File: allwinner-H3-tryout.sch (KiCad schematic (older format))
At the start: 0 parts

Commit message: update,
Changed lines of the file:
@@
 $Descr A4 11693 8268
 encoding utf-8
-Sheet 1 10
+Sheet 1 12
 Title ""
 Date ""
@@
 $EndSheet
 $Sheet
-S 7750 1100 1050 900
+S 8150 1100 1050 900
 U 5C7849B0
 F0 "POWER" 50
@@
 $EndSheet
 $Sheet
-S 7350 4750 1050 900
+S 8150 4750 1050 900
 U 5C1FD862
 F0 "IR" 50
@@
 $EndSheet
 $Sheet
-S 5750 4750 1050 900
+S 6900 4750 1050 900
 U 5C2139DD
 F0 "UART0" 50
@@
 $EndSheet
 $Sheet
-S 4400 4750 1050 900
+S 5650 4750 1050 900
 U 5C21AE0A
 F0 "RTC" 50
@@
 F1 "CSI.sch" 50
 $EndSheet
+$Sheet
+S 8150 2300 1050 900
+U 5C21B42E
+F0 "TF" 50
+F1 "TF.sch" 50
+$EndSheet
+$Sheet
+S 6900 1100 1050 900
+U 5C22EE91
+F0 "USB_POWER" 50
+F1 "USB_POWER.sch" 50
+$EndSheet
+$Sheet
+S 5250 1100 1050 900
+U 5C22DA43
+F0 "eMMC" 50
+F1 "eMMC.sch" 50
+$EndSheet
 $EndSCHEMATC

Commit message: update,
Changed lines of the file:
@@
 $Descr A4 11693 8268
 encoding utf-8
-Sheet 1 12
+Sheet 1 14
 Title ""
 Date ""
@@
 $EndSheet
 $Sheet
-S 5250 1100 1050 900
+S 5650 1100 1050 900
 U 5C22DA43
 F0 "eMMC" 50
 F1 "eMMC.sch" 50
 $EndSheet
+$Sheet
+S 4400 1100 1050 900
+U 5C23FAEA
+F0 "dram" 50
+F1 "dram.sch" 50
+$EndSheet
 $EndSCHEMATC

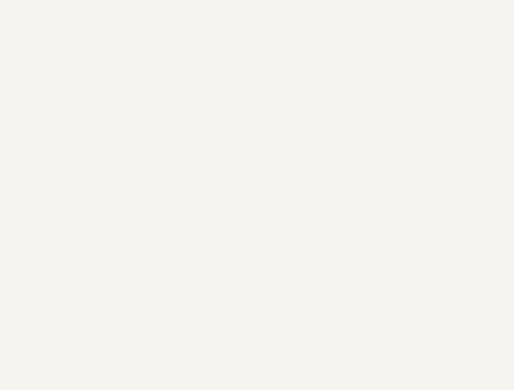
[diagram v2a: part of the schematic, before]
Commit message: udpate mounting hole,
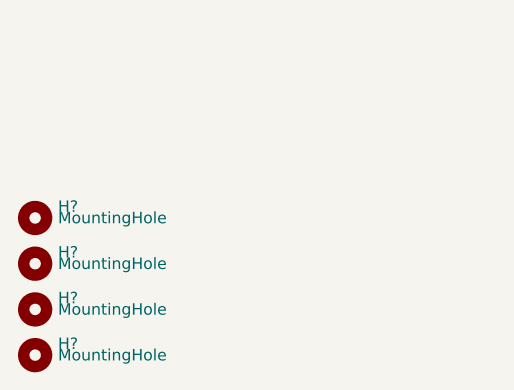
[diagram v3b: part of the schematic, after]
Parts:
- added H? (x3): MountingHole, MountingHole:MountingHole_2.2mm_M2_DIN965, symbol Mechanical:MountingHole
- added H?: MountingHole, MountingHole:MountingHole_2MountingHole:MountingHole_2.2mm_M2_DIN965.2mm_M2_DIN965, symbol Mechanical:MountingHole
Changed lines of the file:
@@
 F1 "dram.sch" 50
 $EndSheet
+$Comp
+L Mechanical:MountingHole H?
+U 1 1 5C5BD210
+P 3950 7000
+F 0 "H?" H 4050 7050 50  0000 L CNN
+F 1 "MountingHole" H 4050 7000 50  0000 L CNN
+F 2 "MountingHole:MountingHole_2.2mm_M2_DIN965" H 3950 7000 50  0001 C CNN
+F 3 "~" H 3950 7000 50  0001 C CNN
+	1    3950 7000
+	1    0    0    -1
+$EndComp
+$Comp
+L Mechanical:MountingHole H?
+U 1 1 5C5BD268
+P 3950 7200
+F 0 "H?" H 4050 7250 50  0000 L CNN
+F 1 "MountingHole" H 4050 7200 50  0000 L CNN
+F 2 "MountingHole:MountingHole_2.2mm_M2_DIN965" H 3950 7200 50  0001 C CNN
+F 3 "~" H 3950 7200 50  0001 C CNN
+	1    3950 7200
+	1    0    0    -1
+$EndComp
+$Comp
+L Mechanical:MountingHole H?
+U 1 1 5C5BD298
+P 3950 7400
+F 0 "H?" H 4050 7450 50  0000 L CNN
+F 1 "MountingHole" H 4050 7400 50  0000 L CNN
+F 2 "MountingHole:MountingHole_2.2mm_M2_DIN965" H 3950 7400 50  0001 C CNN
+F 3 "~" H 3950 7400 50  0001 C CNN
+	1    3950 7400
+	1    0    0    -1
+$EndComp
+$Comp
+L Mechanical:MountingHole H?
+U 1 1 5C5BD2C2
+P 3950 7600
+F 0 "H?" H 4050 7650 50  0000 L CNN
+F 1 "MountingHole" H 4050 7600 50  0000 L CNN
+F 2 "MountingHole:MountingHole_2MountingHole:MountingHole_2.2mm_M2_DIN965.2mm_M2_DIN965" H 3950 7600 50  0001 C CNN
+F 3 "~" H 3950 7600 50  0001 C CNN
+	1    3950 7600
+	1    0    0    -1
+$EndComp
 $EndSCHEMATC

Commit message: update,
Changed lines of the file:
@@
 $Descr A4 11693 8268
 encoding utf-8
-Sheet 1 14
+Sheet 1 15
 Title ""
 Date ""
@@
 	1    0    0    -1
 $EndComp
+$Sheet
+S 600  650  850  400
+U 5C5C55F2
+F0 "cpu-power" 50
+F1 "cpu-power.sch" 50
+$EndSheet
 $EndSCHEMATC

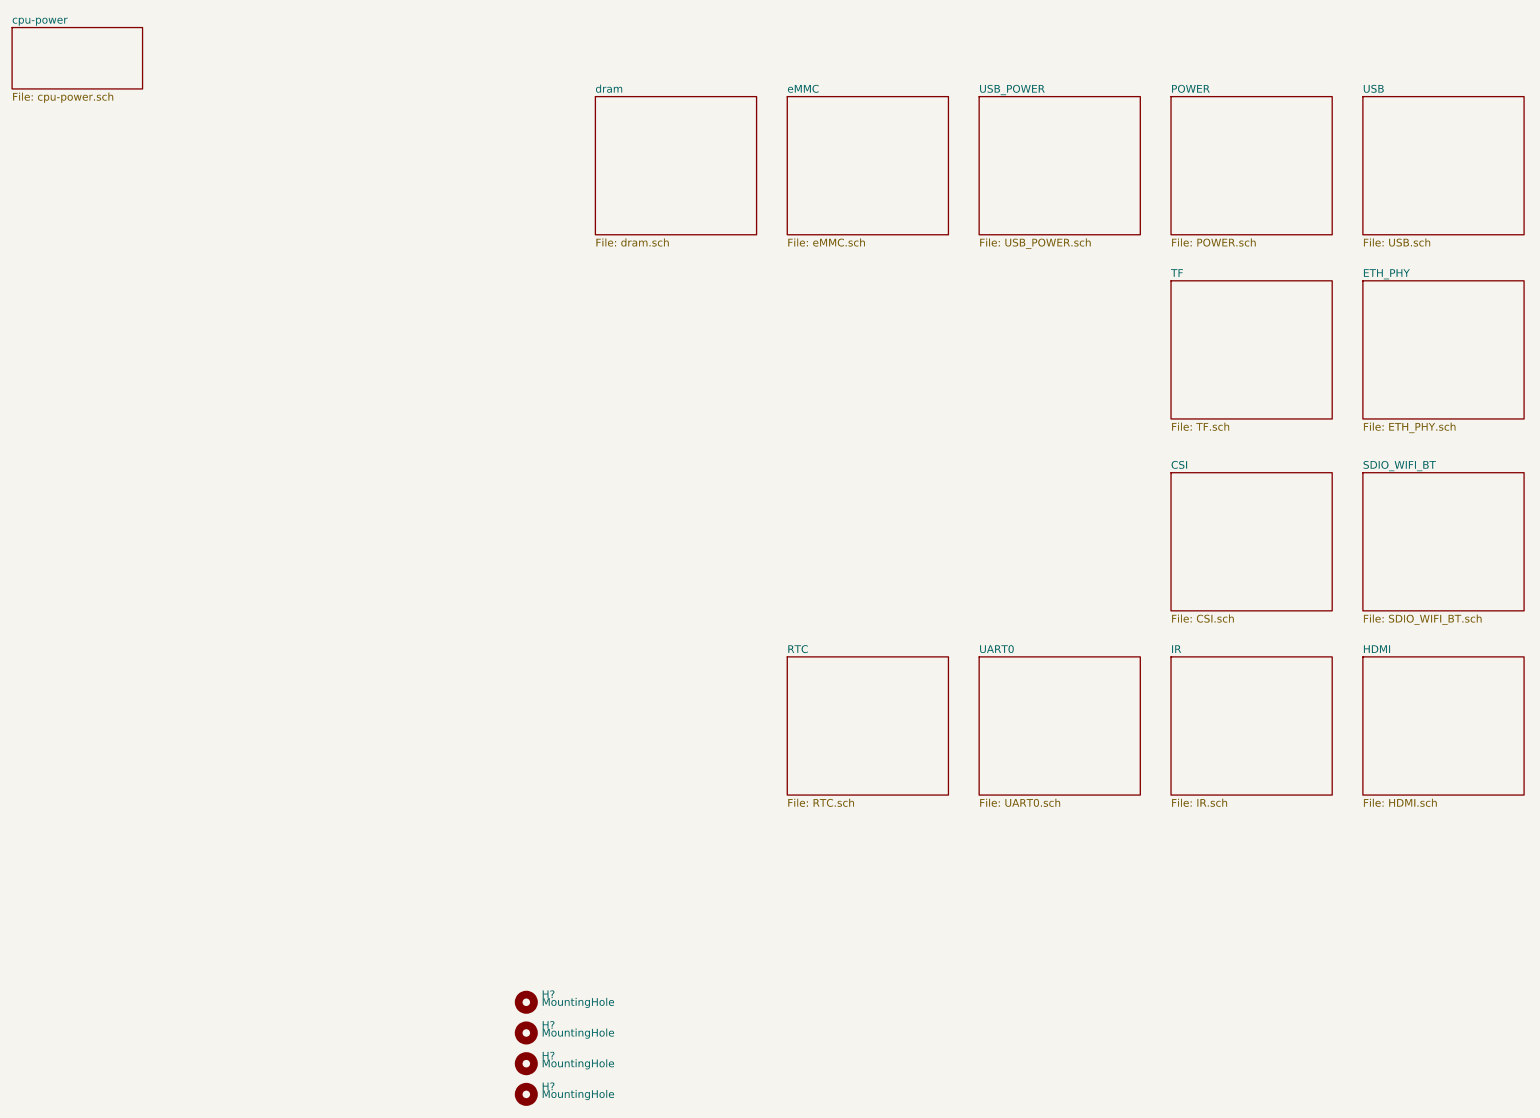
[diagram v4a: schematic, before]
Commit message: update cpu related schematic,
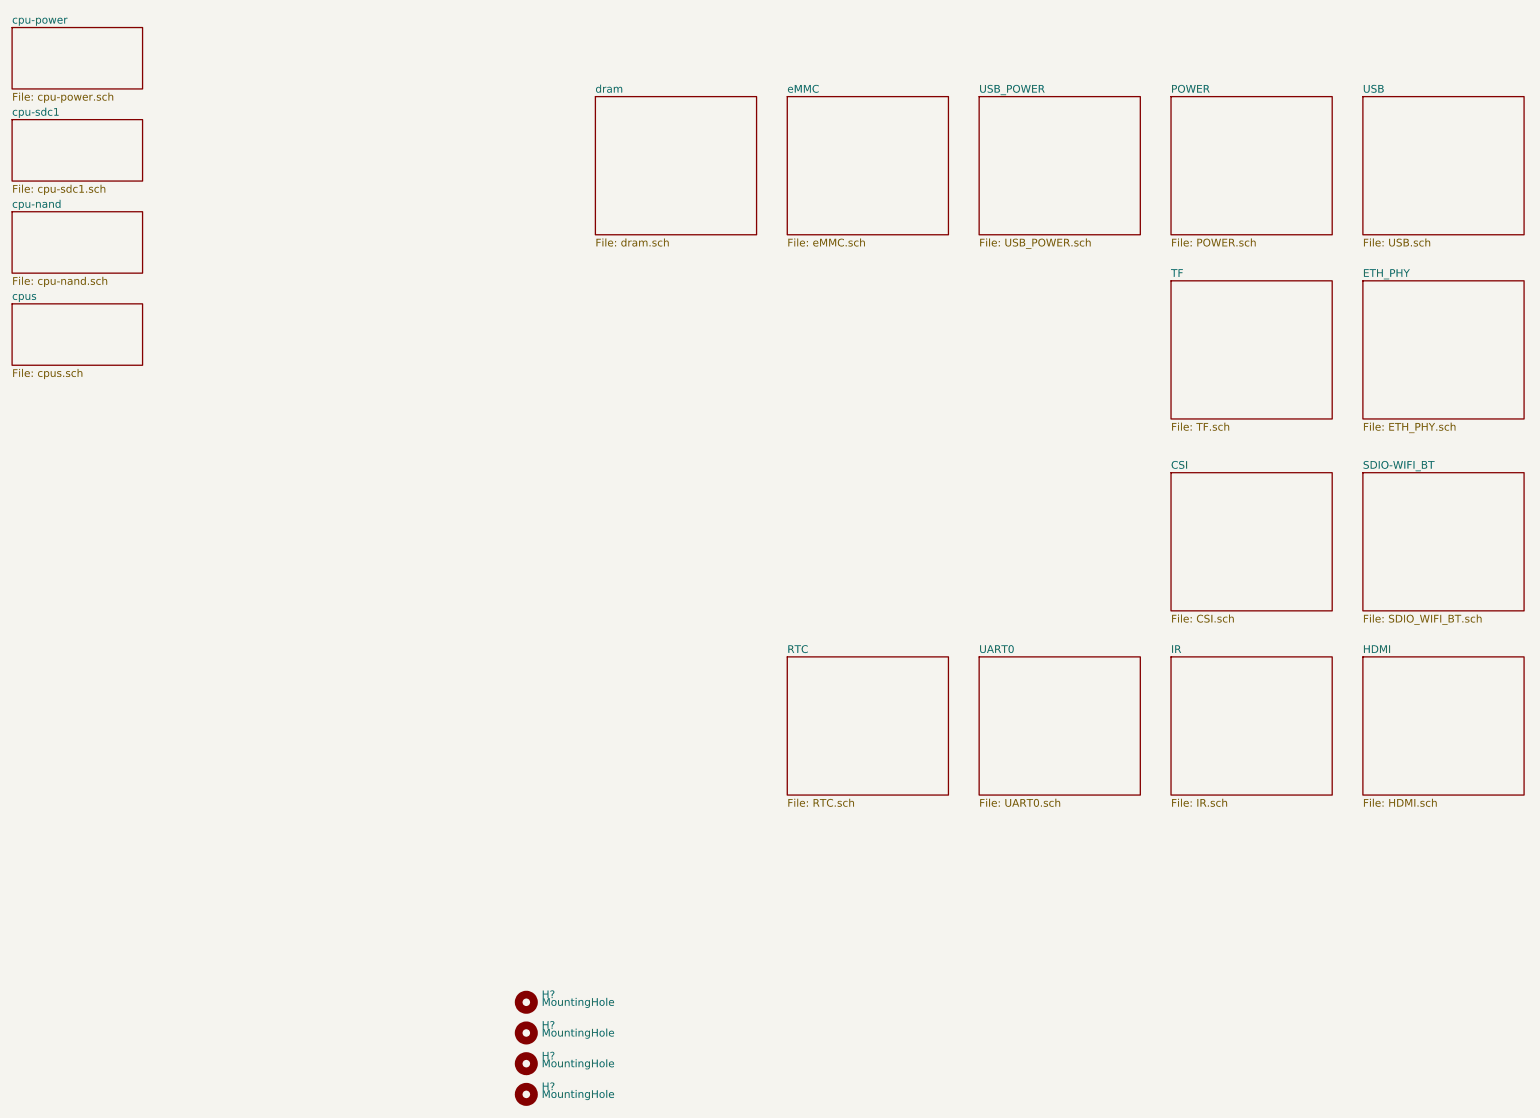
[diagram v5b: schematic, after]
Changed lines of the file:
@@
 $Descr A4 11693 8268
 encoding utf-8
-Sheet 1 15
+Sheet 1 18
 Title ""
 Date ""
@@
 S 9400 3550 1050 900
 U 5C1E10A8
-F0 "SDIO_WIFI_BT" 50
+F0 "SDIO-WIFI_BT" 50
 F1 "SDIO_WIFI_BT.sch" 50
 $EndSheet
@@
 F1 "cpu-power.sch" 50
 $EndSheet
+$Sheet
+S 600  1250 850  400
+U 5C660882
+F0 "cpu-sdc1" 50
+F1 "cpu-sdc1.sch" 50
+$EndSheet
+$Sheet
+S 600  1850 850  400
+U 5C66BA53
+F0 "cpu-nand" 50
+F1 "cpu-nand.sch" 50
+$EndSheet
+$Sheet
+S 600  2450 850  400
+U 5C66D9B1
+F0 "cpus" 50
+F1 "cpus.sch" 50
+$EndSheet
 $EndSCHEMATC
